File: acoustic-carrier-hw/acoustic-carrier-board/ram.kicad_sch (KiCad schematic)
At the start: 15 parts, among them IC1 ECP5-BGA256, U5 MT41K64M16TW-107_J-TR

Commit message: [carrier] Started schematic check, replaced 8 with 16 pin connectors
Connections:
- no-connect marks 0 -> 6
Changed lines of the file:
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@@
 		(color 0 0 0 0)
+	)
+	(no_connect
+		(at 142.24 118.11)
+	)
+	(no_connect
+		(at 142.24 120.65)
+	)
+	(no_connect
+		(at 142.24 123.19)
+	)
+	(no_connect
+		(at 142.24 128.27)
+	)
+	(no_connect
+		(at 142.24 125.73)
+	)
+	(no_connect
+		(at 64.77 91.44)
 	)
 	(wire
@@
 		(on_board yes)
 		(dnp no)
-		(fields_autoplaced yes)
 		(property "Reference" "#PWR02"
 			(at 251.46 41.91 0)
@@
 		)
 		(property "Value" "GND"
-			(at 251.46 40.64 0)
-			(effects
-				(font
+			(at 247.142 38.608 0)
+			(effects
+				(font

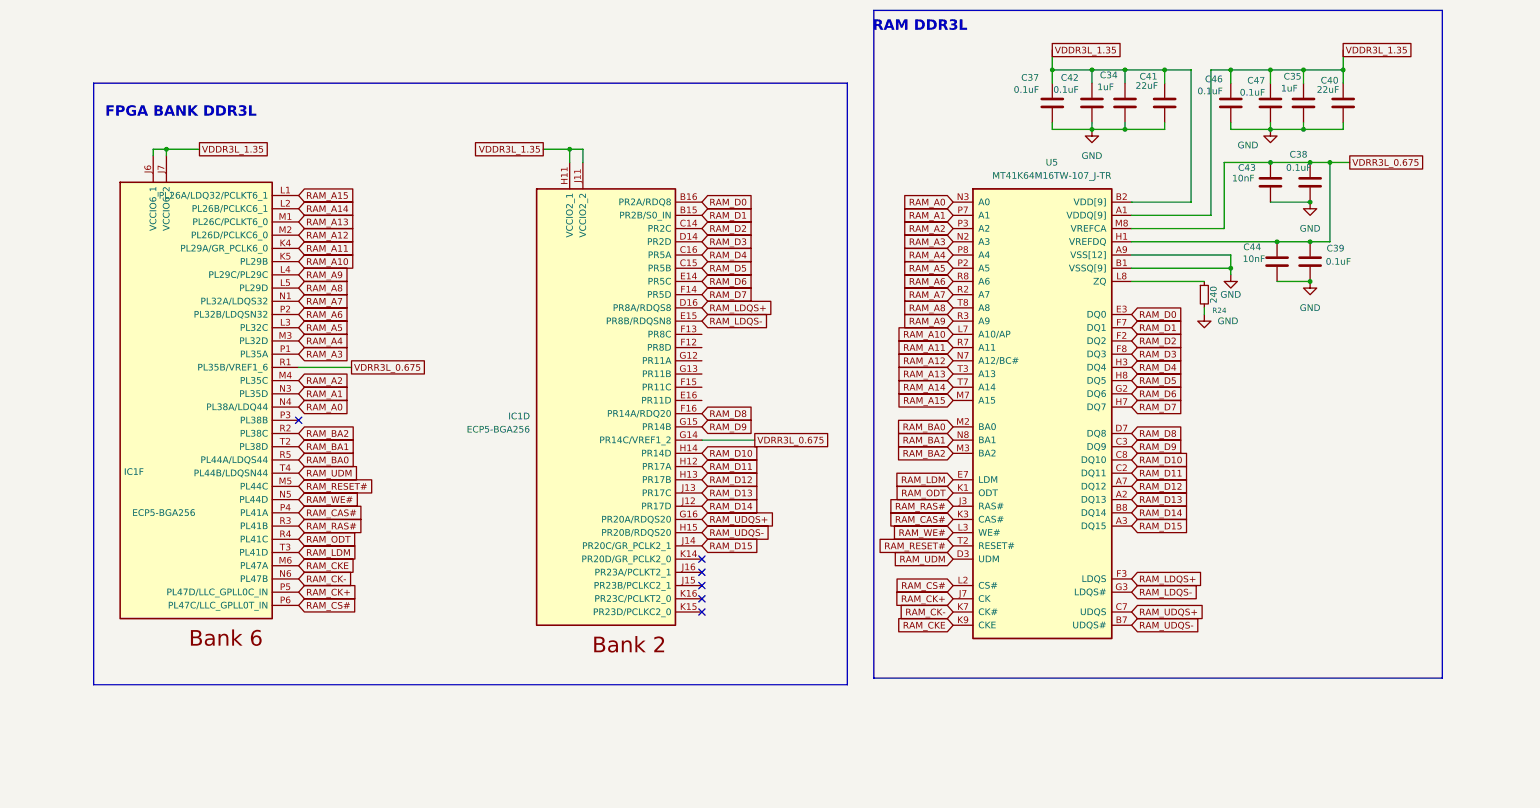
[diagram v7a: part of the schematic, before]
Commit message: [carrier] Fixed most of the carrier board ERC issues (next) fix BGA ERC issue
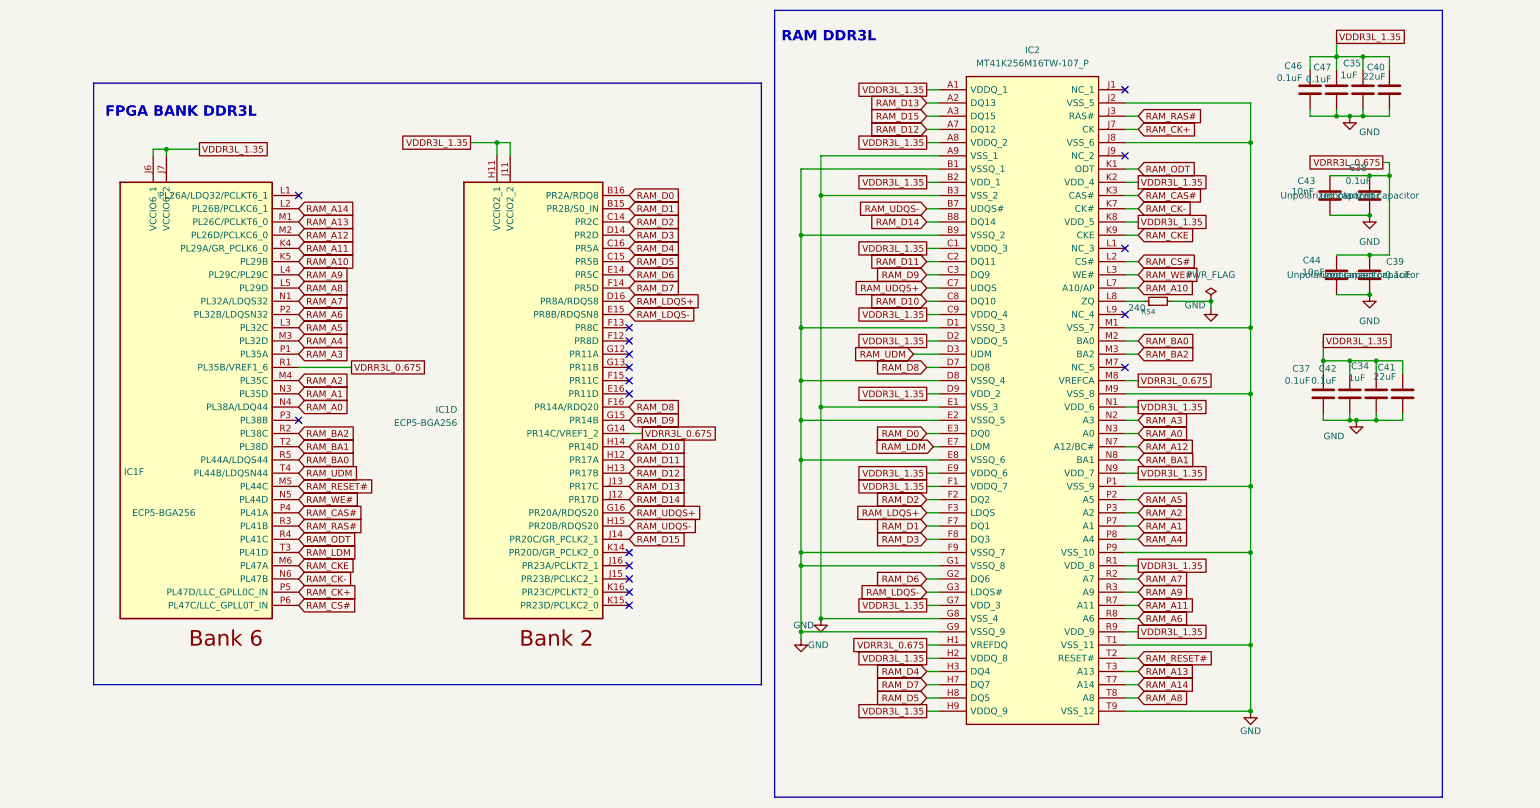
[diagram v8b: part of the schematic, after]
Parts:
- removed R24: 240, Resistor_SMD:R_0603_1608Metric, symbol Device:R_Small
- removed U5: MT41K64M16TW-107_J-TR, Package_BGA:BGA-96_9.0x13.0mm_Layout2x3x16_P0.8mm, symbol gkl_mem:MT41K64M16TW-107_J-TR
- added IC2: MT41K256M16TW-107_P, fpga:BGA96C80P9X16_800X1400X120, symbol MT41K256M16TW-107-P:MT41K256M16TW-107_P
- added R54: 240, Resistor_SMD:R_0603_1608Metric, symbol Device:R_Small
- IC1: footprint BGA256C80P16X16_1400X1400X170 -> fpga:BGA256C80P16X16_1400X1400X170; LPN (none) -> C1521614; MPN (none) -> LFE5U-25F-6BG256C; Part Number LFE5U-12F-6BG256C -> LFE5U-25F-6BG256C
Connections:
- net GND: now also IC2.A9 (VSS_1), IC2.B1 (VSSQ_1), IC2.B3 (VSS_2), IC2.B9 (VSSQ_2), IC2.D1 (VSSQ_3), IC2.D8 (VSSQ_4), IC2.E1 (VSS_3), IC2.E2 (VSSQ_5), IC2.E8 (VSSQ_6), IC2.F9 (VSSQ_7), IC2.G1 (VSSQ_8), IC2.G8 (VSS_4), IC2.G9 (VSSQ_9), IC2.J2 (VSS_5), IC2.J8 (VSS_6), IC2.M1 (VSS_7), IC2.M9 (VSS_8), IC2.P1 (VSS_9), IC2.P9 (VSS_10), IC2.T1 (VSS_11), IC2.T9 (VSS_12), R54.2
- net RAM_A0: now also IC2.N3 (A0)
- net RAM_A1: now also IC2.P7 (A1)
- net RAM_A10: now also IC2.L7 (A10/AP)
- net RAM_A11: now also IC2.R7 (A11)
- net RAM_A12: now also IC2.N7 (A12/BC#)
- net RAM_A13: now also IC2.T3 (A13)
- net RAM_A14: now also IC2.T7 (A14)
- net RAM_A2: now also IC2.P3 (A2)
- net RAM_A3: now also IC2.N2 (A3)
- net RAM_A4: now also IC2.P8 (A4)
- net RAM_A5: now also IC2.P2 (A5)
- net RAM_A6: now also IC2.R8 (A6)
- net RAM_A7: now also IC2.R2 (A7)
- net RAM_A8: now also IC2.T8 (A8)
- net RAM_A9: now also IC2.R3 (A9)
- net RAM_BA0: now also IC2.M2 (BA0)
- net RAM_BA1: now also IC2.N8 (BA1)
- net RAM_BA2: now also IC2.M3 (BA2)
- net RAM_CAS#: now also IC2.K3 (CAS#)
- net RAM_CK+: now also IC2.J7 (CK)
- net RAM_CK-: now also IC2.K7 (CK#)
- net RAM_CKE: now also IC2.K9 (CKE)
- net RAM_CS#: now also IC2.L2 (CS#)
- net RAM_D0: now also IC2.E3 (DQ0)
- net RAM_D1: now also IC2.F7 (DQ1)
- net RAM_D10: now also IC2.C8 (DQ10)
- net RAM_D11: now also IC2.C2 (DQ11)
- net RAM_D12: now also IC2.A7 (DQ12)
- net RAM_D13: now also IC2.A2 (DQ13)
- net RAM_D14: now also IC2.B8 (DQ14)
- net RAM_D15: now also IC2.A3 (DQ15)
- net RAM_D2: now also IC2.F2 (DQ2)
- net RAM_D3: now also IC2.F8 (DQ3)
- net RAM_D4: now also IC2.H3 (DQ4)
- net RAM_D5: now also IC2.H8 (DQ5)
- net RAM_D6: now also IC2.G2 (DQ6)
- net RAM_D7: now also IC2.H7 (DQ7)
- net RAM_D8: now also IC2.D7 (DQ8)
- net RAM_D9: now also IC2.C3 (DQ9)
- net RAM_LDM: now also IC2.E7 (LDM)
- net RAM_LDQS+: now also IC2.F3 (LDQS)
- net RAM_LDQS-: now also IC2.G3 (LDQS#)
- net RAM_ODT: now also IC2.K1 (ODT)
- net RAM_RAS#: now also IC2.J3 (RAS#)
- net RAM_RESET#: now also IC2.T2 (RESET#)
- net RAM_UDM: now also IC2.D3 (UDM)
- net RAM_UDQS+: now also IC2.C7 (UDQS)
- net RAM_UDQS-: now also IC2.B7 (UDQS#)
- net RAM_WE#: now also IC2.L3 (WE#)
- net VDDR3L_1.35: now also IC2.A1 (VDDQ_1), IC2.A8 (VDDQ_2), IC2.B2 (VDD_1), IC2.C1 (VDDQ_3), IC2.C9 (VDDQ_4), IC2.D2 (VDDQ_5), IC2.D9 (VDD_2), IC2.E9 (VDDQ_6), IC2.F1 (VDDQ_7), IC2.G7 (VDD_3), IC2.H2 (VDDQ_8), IC2.H9 (VDDQ_9), IC2.K2 (VDD_4), IC2.K8 (VDD_5), IC2.N1 (VDD_6), IC2.N9 (VDD_7), IC2.R1 (VDD_8), IC2.R9 (VDD_9)
- net VDRR3L_0.675: now also IC2.H1 (VREFDQ), IC2.M8 (VREFCA)
- net RAM_A15: no longer names the net of IC1.L1 (PL26A/LDQ32/PCLKT6_1)
- new net: IC2.L8 (ZQ), R54.1
- no-connect marks 6 -> 18
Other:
- moved on the sheet: C34, C35, C37, C38, C39, C40, C41, C42, C43, C44, C46, C47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
